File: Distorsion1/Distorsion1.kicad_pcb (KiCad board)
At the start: 2 copper layers, 35 x 79.4 mm, 43 parts, among them J1 Jack-DC, J2 IN, J3 OUT, Sw1 Footswitch, U1 TL082

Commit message: PCB 1.0
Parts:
- removed C10: 1uF, Capacitor_SMD:C_0805_2012Metric_Pad1.15x1.40mm_HandSolder
- removed C11: 4.7nF, Capacitor_SMD:C_0805_2012Metric_Pad1.15x1.40mm_HandSolder
- removed C12: 10nF, Capacitor_SMD:C_0805_2012Metric_Pad1.15x1.40mm_HandSolder
- removed G***: LOGO, Aesthetics:frima
- removed J1: Jack-DC, Connector_BarrelJack:BarrelJack_CUI_PJ-102AH_Horizontal
- removed R12: 1K, Resistor_SMD:R_0805_2012Metric_Pad1.15x1.40mm_HandSolder
- removed REF** (x4): MountingHole_2.2mm_M2_Pad_Via, MountingHole:MountingHole_2.2mm_M2_Pad_Via
- added RV5: 100K, Connector_PinSocket_2.54mm:PinSocket_1x03_P2.54mm_Vertical, F.Cu at (191.3, 61.5)
- added Vin1: Con_female, Connector_PinHeader_2.54mm:PinHeader_1x02_P2.54mm_Vertical, F.Cu at (174.0, 28.7)
- C1: footprint Capacitor_Tantalum_SMD:CP_EIA-7343-30_AVX-N_Pad2.25x2.55mm_HandSolder -> Capacitor_SMD:C_0805_2012Metric_Pad1.18x1.45mm_HandSolder; moved to F.Cu
- C2: value 2.2uF -> 22nF; footprint Capacitor_SMD:C_0805_2012Metric_Pad1.15x1.40mm_HandSolder -> Capacitor_SMD:C_0805_2012Metric_Pad1.18x1.45mm_HandSolder; moved to F.Cu
- C3: value 22nF -> 1nF; footprint Capacitor_SMD:C_0805_2012Metric_Pad1.15x1.40mm_HandSolder -> Capacitor_SMD:C_0805_2012Metric_Pad1.18x1.45mm_HandSolder; moved to F.Cu
- C4: value 2.2uF -> 100nF; footprint Capacitor_THT:C_Radial_D5.0mm_H5.0mm_P2.00mm -> Capacitor_SMD:C_0805_2012Metric_Pad1.18x1.45mm_HandSolder
- C5: value 4.7uF -> 100pF; footprint Capacitor_THT:C_Radial_D5.0mm_H5.0mm_P2.00mm -> Capacitor_SMD:C_0805_2012Metric_Pad1.18x1.45mm_HandSolder
- C6: value 4.7uF -> 1uF; footprint Capacitor_SMD:C_0805_2012Metric_Pad1.15x1.40mm_HandSolder -> Capacitor_Tantalum_SMD:CP_EIA-3216-18_Kemet-A_Pad1.58x1.35mm_HandSolder; moved to F.Cu
- C7: value 1nF -> 1uF; footprint Capacitor_SMD:C_0805_2012Metric_Pad1.15x1.40mm_HandSolder -> Capacitor_SMD:C_0805_2012Metric_Pad1.18x1.45mm_HandSolder; moved to F.Cu
- C8: value 100pF -> 4.7nF; footprint Capacitor_SMD:C_0805_2012Metric_Pad1.15x1.40mm_HandSolder -> Capacitor_SMD:C_0805_2012Metric_Pad1.18x1.45mm_HandSolder; moved to F.Cu
- C9: value 1uF -> 10nF; footprint Capacitor_Tantalum_SMD:CP_EIA-3216-18_Kemet-A_Pad1.58x1.35mm_HandSolder -> Capacitor_SMD:C_0805_2012Metric_Pad1.18x1.45mm_HandSolder; moved to F.Cu
- D1, D2, D4, D5, U1: moved to F.Cu
- D3, D6: moved to B.Cu
- J2, J3: footprint SamacSys_Parts:NYS2162U -> Distorsion1:NYS2162U
- R1, R11, R2, R3: footprint Resistor_SMD:R_0805_2012Metric_Pad1.15x1.40mm_HandSolder -> Resistor_SMD:R_0805_2012Metric_Pad1.20x1.40mm_HandSolder; moved to F.Cu
- R10: value 22K -> 1K; footprint Resistor_SMD:R_0805_2012Metric_Pad1.15x1.40mm_HandSolder -> Resistor_SMD:R_0805_2012Metric_Pad1.20x1.40mm_HandSolder
- R4: value 27K -> 1K; footprint Resistor_SMD:R_0805_2012Metric_Pad1.15x1.40mm_HandSolder -> Resistor_SMD:R_0805_2012Metric_Pad1.20x1.40mm_HandSolder
- R5: value 27K -> 39K; footprint Resistor_SMD:R_0805_2012Metric_Pad1.15x1.40mm_HandSolder -> Resistor_SMD:R_0805_2012Metric_Pad1.20x1.40mm_HandSolder; moved to F.Cu
- R6: value 47R -> 22K; footprint Resistor_SMD:R_0805_2012Metric_Pad1.15x1.40mm_HandSolder -> Resistor_SMD:R_0805_2012Metric_Pad1.20x1.40mm_HandSolder; moved to F.Cu
- R7: value 560R -> 1K; footprint Resistor_SMD:R_0805_2012Metric_Pad1.15x1.40mm_HandSolder -> Resistor_SMD:R_0805_2012Metric_Pad1.20x1.40mm_HandSolder; moved to F.Cu
- R8: value 1K -> 27K; footprint Resistor_SMD:R_0805_2012Metric_Pad1.15x1.40mm_HandSolder -> Resistor_SMD:R_0805_2012Metric_Pad1.20x1.40mm_HandSolder
- R9: value 39K -> 27K; footprint Resistor_SMD:R_0805_2012Metric_Pad1.15x1.40mm_HandSolder -> Resistor_SMD:R_0805_2012Metric_Pad1.20x1.40mm_HandSolder; moved to F.Cu
- RV1: value 100K -> 10K
- Sw1: footprint SamacSys_Parts:FS57003PLT2B2M2QE -> Distorsion1:FS57003PLT2B2M2QE
- moved R5 118.5 mm to (197.5, 33.2), turned to 0 degrees
- moved R7 106.7 mm to (192.3, 39.1), turned to 0 degrees
- moved C9 101.7 mm to (193.2, 33.2), turned to 0 degrees
- moved R2 100.8 mm to (179.6, 42.9), turned to 270 degrees
- moved U1 99.9 mm to (188.2, 41.9)
- moved R3 99.8 mm to (180.6, 46.5), turned to 180 degrees
- moved C3 99.3 mm to (180.6, 49.0), turned to 0 degrees
- moved D4 99.2 mm to (197.6, 35.1), turned to 180 degrees
- moved R1 98.9 mm to (173.0, 44.9), turned to 90 degrees
- moved D5 98.3 mm to (197.5, 37.6), turned to 0 degrees
- moved RV2 96.4 mm to (191.3, 51.3), turned to 0 degrees
- moved C5 96.2 mm to (187.5, 51.3), turned to 180 degrees
- moved C2 94.0 mm to (176.6, 44.9), turned to 270 degrees
- moved C7 93.0 mm to (180.9, 54.4), turned to 0 degrees
- moved D2 92.4 mm to (187.5, 47.5), turned to 180 degrees
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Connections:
- C2 pad 2: GND -> Net-(C2-Pad2)
- C3 pad 1: Net-(C3-Pad1) -> GND
- C4 pad 1: Net-(C2-Pad1) -> GND
- C4 pad 2: GND -> Net-(C4-Pad2)
- C5 pad 2: GND -> Net-(C5-Pad2)
- C6 pad 1: Net-(C5-Pad1) -> Net-(C6-Pad1)
- C6 pad 2: GND -> Net-(C5-Pad2)
- C7 pad 1: GND -> Net-(C6-Pad1)
- C7 pad 2: Net-(C7-Pad2) -> Net-(C5-Pad2)
- C8 pad 1: Net-(C8-Pad1) -> Net-(C6-Pad1)
- C8 pad 2: Net-(C10-Pad2) -> Net-(C8-Pad2)
- C9 pad 1: Net-(C10-Pad1) -> GND
- C9 pad 2: Net-(C10-Pad2) -> Net-(C9-Pad2)
- D1 pad 1: Net-(C10-Pad2) -> Net-(C5-Pad2)
- D1 pad 2: Net-(C8-Pad1) -> Net-(C5-Pad1)
- D2 pad 1: Net-(C8-Pad1) -> Net-(C5-Pad1)
- D2 pad 2: Net-(C10-Pad2) -> Net-(C5-Pad2)
- D4 pad 1: Net-(C10-Pad1) -> Net-(C6-Pad1)
- D5 pad 2: Net-(C10-Pad1) -> Net-(C6-Pad1)
- R1 pad 1: Net-(C3-Pad2) -> Net-(C2-Pad2)
- R10 pad 2: Net-(C11-Pad2) -> Net-(D3-Pad1)
- R11 pad 1: Net-(R11-Pad1) -> GND
- R2 pad 2: Net-(C3-Pad1) -> Net-(C2-Pad1)
- R3 pad 1: Net-(C7-Pad2) -> Net-(C3-Pad2)
- R3 pad 2: Net-(C3-Pad1) -> Net-(C2-Pad1)
- R4 pad 1: +12V -> Net-(C5-Pad1)
- R4 pad 2: +6V -> Net-(R4-Pad2)
- R5 pad 1: +6V -> Net-(C9-Pad2)
- R5 pad 2: GND -> Net-(C6-Pad1)
- R6 pad 1: Net-(C8-Pad1) -> GND
- R6 pad 2: Net-(C2-Pad1) -> Net-(C8-Pad2)
- R7 pad 1: Net-(C8-Pad1) -> Net-(R7-Pad1)
- R7 pad 2: Net-(C5-Pad1) -> Net-(R7-Pad2)
- R8 pad 1: GND -> +12V
- R8 pad 2: Net-(D3-Pad1) -> +6V
- R9 pad 1: Net-(C12-Pad2) -> +6V
- R9 pad 2: Net-(C10-Pad1) -> GND
- RV1 pad 1: Net-(C8-Pad1) -> Net-(R4-Pad2)
- RV1 pad 2: Net-(C10-Pad2) -> Net-(C4-Pad2)
- RV1 pad 3: Net-(C10-Pad2) -> Net-(C4-Pad2)
- RV2 pad 1: Net-(C12-Pad2) -> Net-(C5-Pad1)
- RV2 pad 2: Net-(R11-Pad2) -> Net-(C5-Pad2)
- RV2 pad 3: Net-(C11-Pad2) -> Net-(C5-Pad2)
- RV3 pad 1: Net-(R11-Pad1) -> Net-(C9-Pad2)
- RV3 pad 2: Net-(RV3-Pad2) -> Net-(R7-Pad2)
- RV3 pad 3: GND -> Net-(C8-Pad2)
- Sw1 pad 3: Net-(C3-Pad2) -> Net-(C2-Pad2)
- Sw1 pad 4: (no net) -> Net-(Sw1-Pad4)
- Sw1 pad 5: Net-(R12-Pad2) -> Net-(R11-Pad2)
- Sw1 pad 9: Net-(RV3-Pad2) -> Net-(RV5-Pad2)
- U1 pad 1: Net-(C10-Pad2) -> Net-(C5-Pad2)
- U1 pad 2: Net-(C8-Pad1) -> Net-(C5-Pad1)
- U1 pad 3: Net-(C7-Pad2) -> Net-(C3-Pad2)
- U1 pad 5: (no net) -> Net-(R7-Pad1)
- U1 pad 6: (no net) -> Net-(RV5-Pad1)
- U1 pad 7: (no net) -> Net-(RV5-Pad1)
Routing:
- net GND: track 16.9 -> 182.2 mm, vias 7 -> 0
- net +12V: track 132.2 -> 43.3 mm, vias 2 -> 1
- net Net-(C9-Pad2): track 0.00 -> 77.6 mm
- net Net-(R7-Pad2): track 0.00 -> 58.1 mm
- net Net-(RV5-Pad2): track 0.00 -> 49.4 mm
- net Net-(D6-Pad1): track 73.9 -> 25.8 mm
- net Net-(C8-Pad2): track 0.00 -> 44.7 mm
- net Net-(C6-Pad1): track 0.00 -> 42.8 mm, vias 0 -> 2
- net Net-(C8-Pad1): track 40.9 -> 0.00 mm
- net Net-(C10-Pad2): track 31.4 -> 0.00 mm
- net Net-(C4-Pad2): track 0.00 -> 30.6 mm
- net Net-(C5-Pad1): track 3.64 -> 32.9 mm
- net Net-(RV3-Pad2): track 27.4 -> 0.00 mm
- net Net-(RV5-Pad1): track 0.00 -> 25.2 mm, vias 0 -> 1
- net Net-(C5-Pad2): track 0.00 -> 22.6 mm
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- removed copper zone on B.Cu, net GND
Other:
- board outline removed
- net class Default: trace_width 0.3 -> 0.2
- board text removed: "Distortion One"
- board text removed: "Gain"
- board text removed: "Tone"
- board text removed: "V1.0"
- board text removed: "Volume"

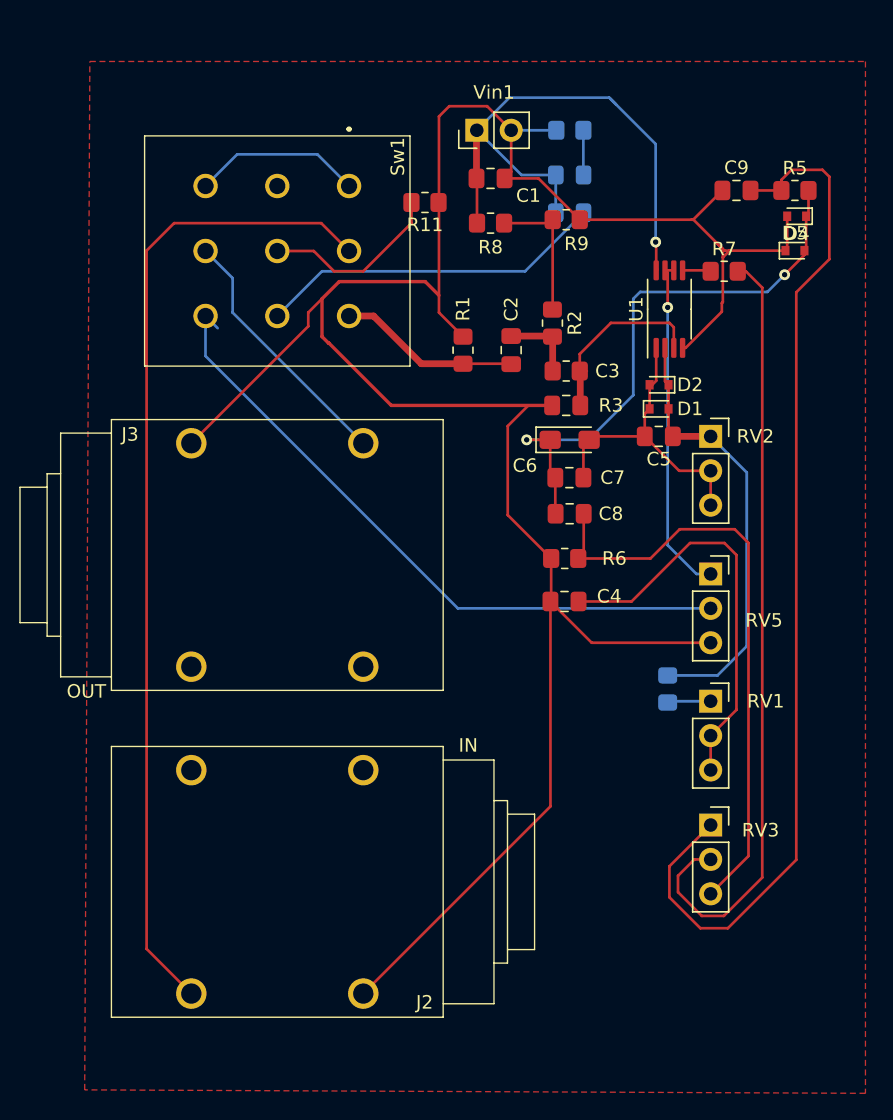
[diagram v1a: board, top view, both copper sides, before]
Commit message: PCB1.1(Aumento de pistas de 0.2 a 0.5)
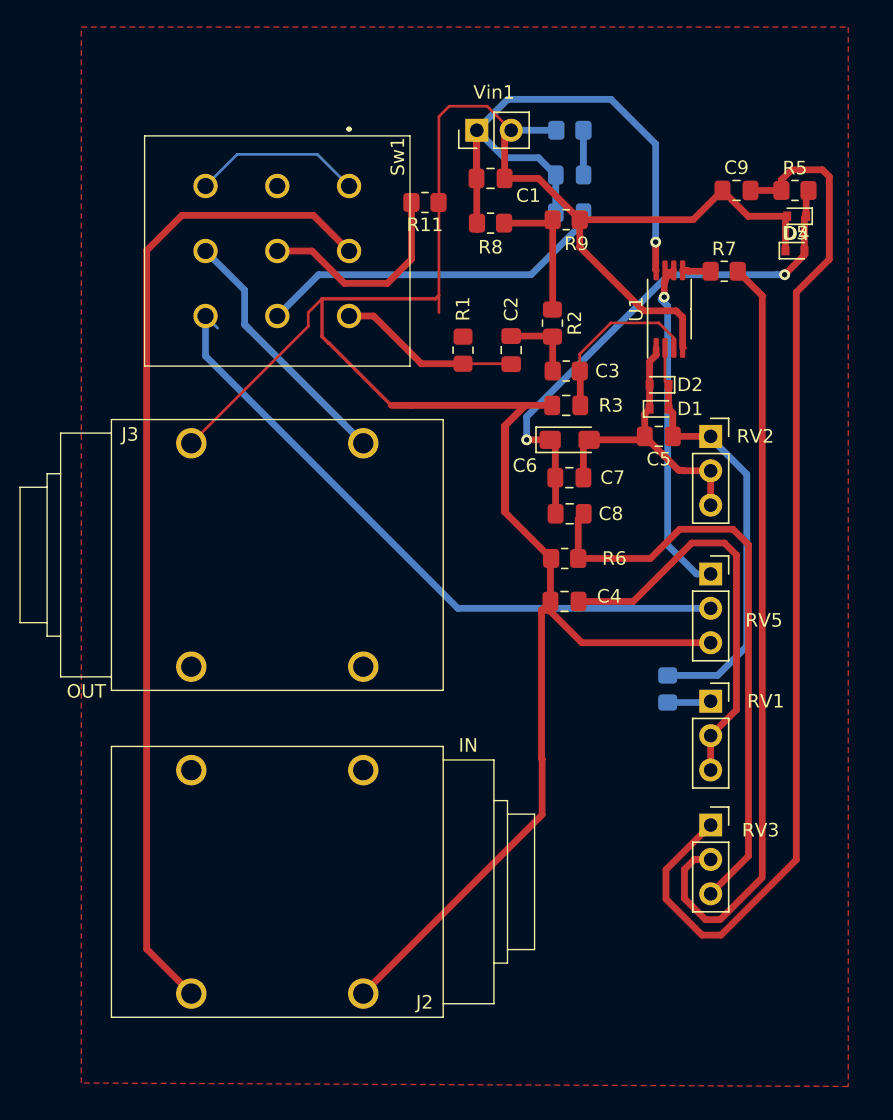
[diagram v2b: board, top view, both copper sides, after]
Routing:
- net GND: track 182.2 -> 203.8 mm
- net +12V: track 43.3 -> 62.9 mm
- net Net-(J3-Pad1): track 19.3 -> 31.7 mm
- net Net-(C6-Pad1): track 42.8 -> 39.6 mm
- net Net-(RV5-Pad1): track 25.2 -> 27.7 mm
- net Net-(R11-Pad2): track 13.8 -> 16.1 mm
- net Net-(C9-Pad2): track 77.6 -> 78.4 mm
- net Net-(R7-Pad2): track 58.1 -> 57.6 mm

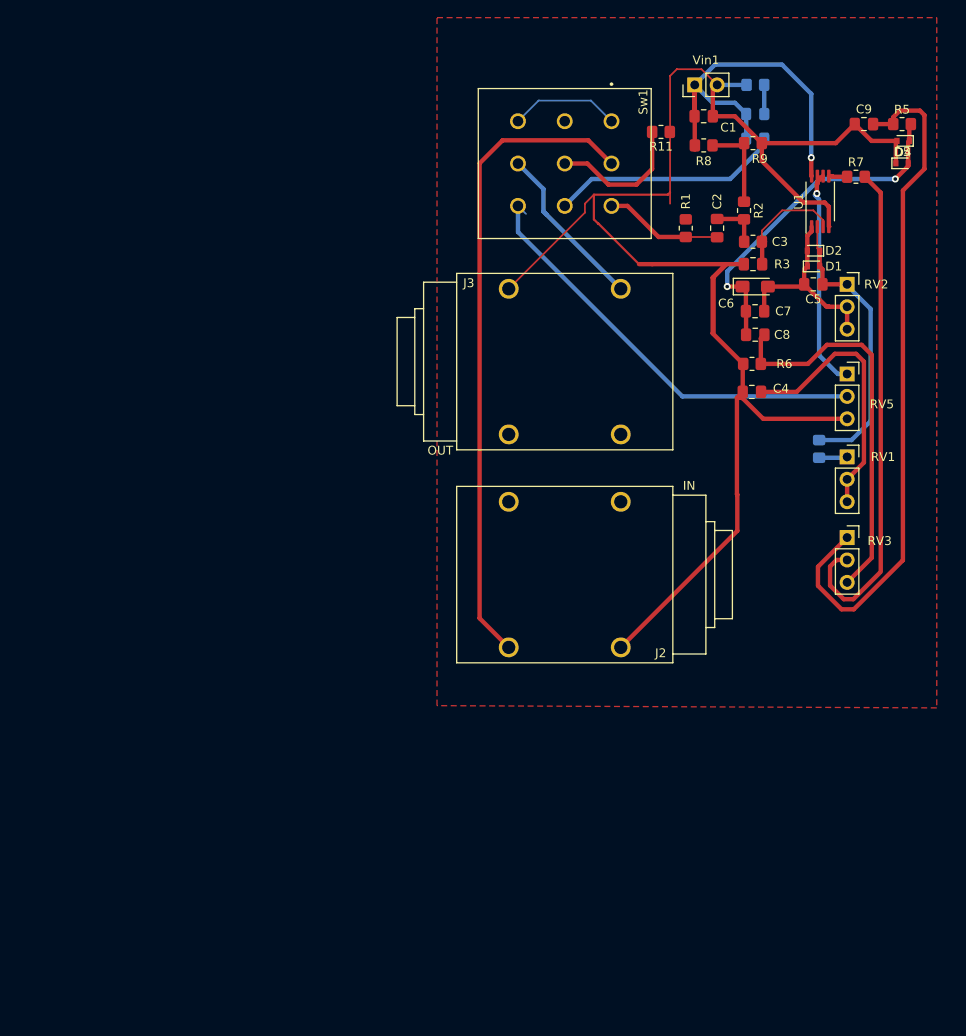
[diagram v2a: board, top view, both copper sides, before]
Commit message: PCB1.2(Cambio lugar de pot)
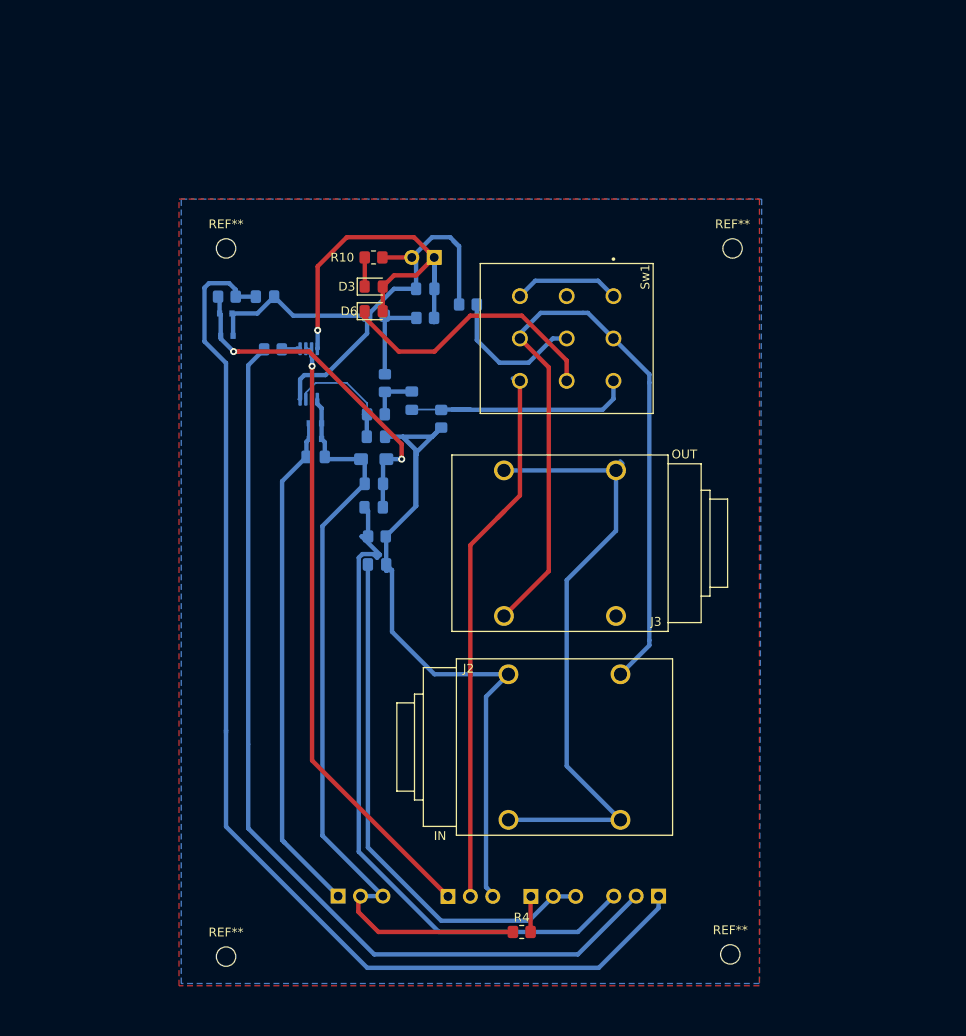
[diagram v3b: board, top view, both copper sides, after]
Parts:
- added REF**: MountingHole_2.2mm_M2_ISO7380, MountingHole:MountingHole_2.2mm_M2_ISO7380, F.Cu at (178.3, 47.2)
- added REF**: MountingHole_2.2mm_M2_ISO7380, MountingHole:MountingHole_2.2mm_M2_ISO7380, F.Cu at (120.9, 47.2)
- added REF**: MountingHole_2.2mm_M2_ISO7380, MountingHole:MountingHole_2.2mm_M2_ISO7380, F.Cu at (120.9, 127.5)
- added REF**: MountingHole_2.2mm_M2_ISO7380, MountingHole:MountingHole_2.2mm_M2_ISO7380, F.Cu at (178.1, 127.3)
- C1, C2, C3, C4, C5, C6, C7, C8, C9, D1, D2, D4, D5, R1, R11, R2, R3, R5, R6, R7, R8, R9, RV1, RV2, RV3, RV5, U1, Vin1: moved to B.Cu
- D3, D6, R10, R4: moved to F.Cu
- moved RV2 90.2 mm to (133.6, 120.7), turned to 270 degrees
- moved D4 79.2 mm to (120.9, 54.6), turned to 0 degrees
- moved D5 79.0 mm to (121.0, 57.2), turned to 180 degrees
- moved R5 79.0 mm to (121.0, 52.7), turned to 180 degrees
- moved RV5 74.5 mm to (146.1, 120.7), turned to 270 degrees
- moved C9 70.6 mm to (125.3, 52.7), turned to 180 degrees
- moved R7 68.9 mm to (126.2, 58.7), turned to 180 degrees
- moved R4 64.3 mm to (154.4, 124.7), turned to 0 degrees
- moved RV1 61.4 mm to (155.5, 120.7), turned to 270 degrees
- moved U1 61.2 mm to (130.3, 61.5)
- moved D1 59.7 mm to (131.0, 68.8), turned to 180 degrees
- moved D2 59.7 mm to (131.0, 67.1), turned to 0 degrees
- moved C5 59.7 mm to (131.1, 70.9), turned to 0 degrees
- moved R10 47.5 mm to (137.6, 48.3), turned to 180 degrees
- moved C6 47.5 mm to (137.6, 71.1), turned to 180 degrees
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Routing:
- net (no net): track 0.00 -> 70.5 mm
- net Net-(C9-Pad2): track 78.4 -> 129.3 mm
- net Net-(R7-Pad2): track 57.6 -> 107.8 mm
- net Net-(C5-Pad1): track 32.9 -> 81.0 mm
- net Net-(C5-Pad2): track 22.5 -> 68.5 mm
- net Net-(RV5-Pad1): track 27.7 -> 71.9 mm
- net GND: track 203.8 -> 167.4 mm
- net Net-(C8-Pad2): track 44.6 -> 78.0 mm
- net Net-(C4-Pad2): track 30.6 -> 60.4 mm
- net Net-(J2-Pad1): track 73.4 -> 54.3 mm
- net Net-(C2-Pad2): track 14.0 -> 27.4 mm
- net Net-(RV5-Pad2): track 49.4 -> 62.4 mm
- net Net-(D6-Pad1): track 26.2 -> 31.3 mm
- net Net-(J3-Pad1): track 31.7 -> 34.8 mm
- net Net-(R11-Pad2): track 16.1 -> 16.7 mm
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- added copper zone on F.Cu, net (none)
- added copper zone on B.Cu, net GND
- removed copper zone on F.Cu, net GND

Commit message: PCB2.0 Nuevo diseño
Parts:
- removed the REF** at (178.3, 47.2)
- removed the REF** at (120.9, 47.2)
- removed the REF** at (120.9, 127.5)
- removed the REF** at (178.1, 127.3)
- removed Vin1: Con_female, Connector_PinHeader_2.54mm:PinHeader_1x02_P2.54mm_Vertical
- added G***: LOGO, Aesthetics:frima, F.Cu at (113.0, 65.5)
- added J1: Jack-DC, Connector_BarrelJack:BarrelJack_CUI_PJ-102AH_Horizontal, F.Cu at (123.9, 120.6)
- added REF**: MountingHole_2.2mm_M2_Pad_Via, MountingHole:MountingHole_2.2mm_M2_Pad_Via, F.Cu at (139.0, 128.0)
- added REF**: MountingHole_2.2mm_M2_Pad_Via, MountingHole:MountingHole_2.2mm_M2_Pad_Via, F.Cu at (139.0, 55.0)
- added REF**: MountingHole_2.2mm_M2_Pad_Via, MountingHole:MountingHole_2.2mm_M2_Pad_Via, F.Cu at (110.0, 55.0)
- C1, R11, R7, RV1, RV2, RV3, RV5: moved to F.Cu
- R4: moved to B.Cu
- moved R10 76.5 mm to (132.8, 124.6), turned to 0 degrees
- moved C1 74.9 mm to (116.2, 121.6), turned to 270 degrees
- moved R7 71.8 mm to (112.0, 129.0)
- moved D3 71.2 mm to (132.8, 122.6), turned to 180 degrees
- moved U1 66.8 mm to (129.5, 128.3), turned to 180 degrees
- moved R9 65.6 mm to (129.3, 120.0)
- moved R8 64.5 mm to (129.3, 118.0), turned to 0 degrees
- moved Sw1 63.2 mm to (123.3, 108.9), turned to 0 degrees
- moved RV3 62.9 mm to (109.3, 103.9), turned to 0 degrees
- moved D6 58.4 mm to (135.3, 112.7), turned to 270 degrees
- moved R1 56.9 mm to (136.1, 122.8)
- moved R2 56.9 mm to (132.2, 119.0)
- moved D2 55.4 mm to (115.1, 120.2), turned to 180 degrees
- moved D1 55.1 mm to (115.1, 121.5), turned to 0 degrees
- moved C2 54.8 mm to (136.1, 119.0)
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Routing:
- net Net-(C9-Pad2): track 129.3 -> 24.9 mm
- net Net-(R7-Pad2): track 107.8 -> 24.7 mm
- net (no net): track 70.5 -> 0.00 mm
- net Net-(C4-Pad2): track 60.4 -> 5.54 mm
- net Net-(RV5-Pad2): track 62.4 -> 7.73 mm
- net Net-(C5-Pad1): track 81.0 -> 33.7 mm
- net Net-(C8-Pad2): track 78.0 -> 34.4 mm, vias 0 -> 1
- net Net-(RV5-Pad1): track 71.9 -> 39.0 mm
- net GND: track 167.4 -> 192.0 mm, vias 0 -> 1
- net Net-(C5-Pad2): track 68.5 -> 45.7 mm
- net Net-(J3-Pad1): track 34.8 -> 54.6 mm
- net +12V: track 62.9 -> 47.5 mm
- net Net-(R7-Pad1): track 2.38 -> 15.0 mm, vias 0 -> 1
- net Net-(C6-Pad1): track 39.6 -> 27.6 mm, vias 2 -> 0
- net Net-(D6-Pad1): track 31.3 -> 20.9 mm
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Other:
- board outline added: 35 x 79.4 mm
- net class Default: trace_width 0.2 -> 0.3
- board text added: "Distortion One"
- board text added: "V1.0"
